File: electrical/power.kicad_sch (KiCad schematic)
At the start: 58 parts

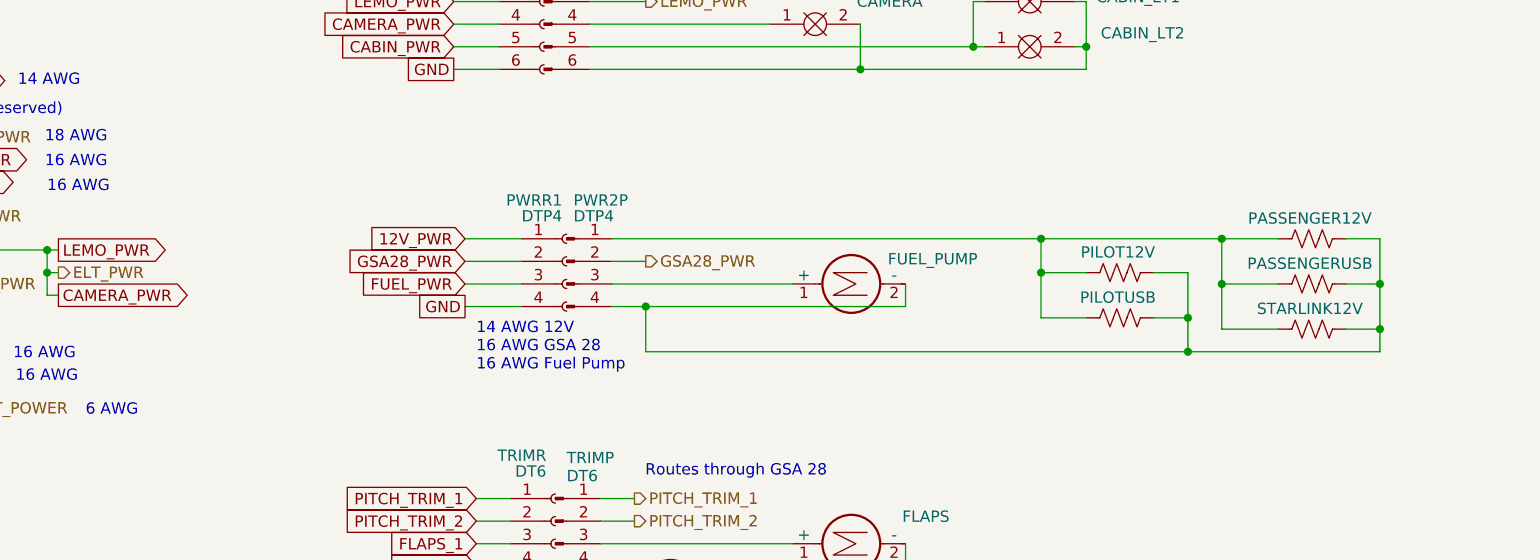
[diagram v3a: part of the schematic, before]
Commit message: Moved pilot USB to be before connector to match wiring.
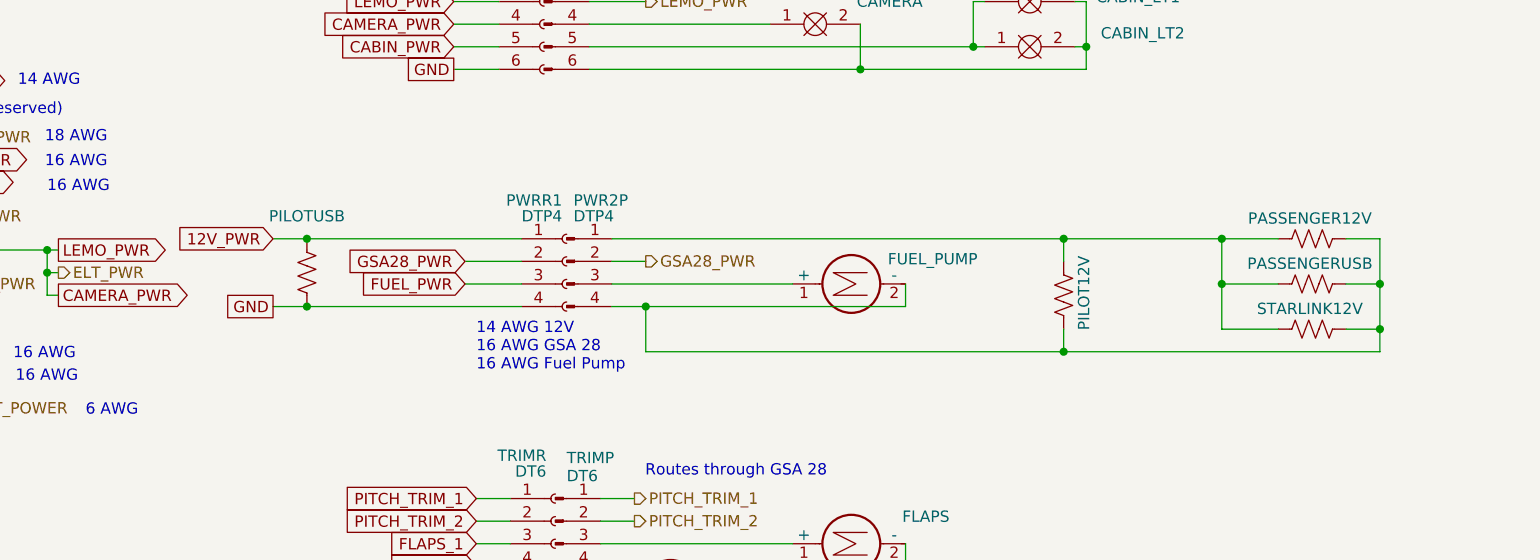
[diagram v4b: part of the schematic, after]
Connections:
- net 12V_PWR: now also PILOTUSB.2
- net GND: now also PILOTUSB.1
- net at FUEL_PUMP.2 (-), PASSENGER12V.1, PASSENGERUSB.1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: no longer PILOTUSB.1
- net at PASSENGER12V.2, PASSENGERUSB.2, PILOT12V.2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: no longer PILOTUSB.2
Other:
- moved on the sheet: PILOT12V, PILOTUSB
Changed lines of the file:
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@@
 	(title_block
 		(title "Power Distribution")
-		(date "2025-10-12")
-		(rev "1.1.8")
+		(date "2025-10-13")
+		(rev "1.1.10")
 		(company "N78HR")
 	)
@@
 	)
 	(junction
+		(at 193.04 224.79)
+		(diameter 0)
+		(color 0 0 0 0)
+	)
+	(junction
 		(at 180.34 153.67)
 		(diameter 0)
@@
 	)
 	(junction
-		(at 190.5 215.9)
-		(diameter 0)
-		(color 0 0 0 0)
-	)
-	(junction
 		(at 69.85 283.21)
 		(diameter 0)
@@
 	)
 	(junction
-		(at 207.01 220.98)
-		(diameter 0)
-		(color 0 0 0 0)
-	)
-	(junction
 		(at 99.06 341.63)
 		(diameter 0)
@@
 	)
 	(junction
+		(at 107.95 219.71)
+		(diameter 0)
+		(color 0 0 0 0)
+	)
+	(junction
 		(at 86.36 350.52)
 		(diameter 0)
@@
 	)
 	(junction
+		(at 107.95 212.09)
+		(diameter 0)
+		(color 0 0 0 0)
+	)
+	(junction
 		(at 162.56 22.86)
 		(diameter 0)
@@
 	)
 	(junction
-		(at 190.5 212.09)
-		(diameter 0)
-		(color 0 0 0 0)
-	)
-	(junction
 		(at 167.64 85.09)
 		(diameter 0)
@@
 	)
 	(junction
-		(at 207.01 224.79)
-		(diameter 0)
-		(color 0 0 0 0)
-	)
-	(junction
 		(at 86.36 336.55)
 		(diameter 0)
@@
 		(color 0 0 0 0)
 	)
+	(junction
+		(at 193.04 212.09)
+		(diameter 0)
+		(color 0 0 0 0)
+	)
 	(no_connect
 		(at 166.37 39.37)
@@
 	(wire
 		(pts
-			(xy 125.73 212.09) (xy 132.08 212.09)
+			(xy 104.14 212.09) (xy 107.95 212.09)
 		)
 		(stroke
@@
 	(wire
 		(pts
-			(xy 207.01 224.79) (xy 228.6 224.79)
+			(xy 146.05 224.79) (xy 193.04 224.79)
 		)
 		(stroke
@@
 	(wire
 		(pts
-			(xy 190.5 215.9) (xy 190.5 212.09)
-		)
-		(stroke
-			(width 0)
-			(type default)
-		)
-	)
-	(wire
-		(pts
 			(xy 195.58 193.04) (xy 195.58 190.5)
 		)
@@
 	(wire
 		(pts
-			(xy 190.5 220.98) (xy 195.58 220.98)
-		)
-		(stroke
-			(width 0)
-			(type default)
-		)
-	)
-	(wire
-		(pts
 			(xy 133.35 80.01) (xy 167.64 80.01)
 		)
@@
 	(wire
 		(pts
-			(xy 190.5 215.9) (xy 190.5 220.98)
-		)
-		(stroke
-			(width 0)
-			(type default)
-		)
-	)
-	(wire
-		(pts
 			(xy 106.68 314.96) (xy 102.87 314.96)
 		)
@@
 	(wire
 		(pts
+			(xy 107.95 212.09) (xy 132.08 212.09)
+		)
+		(stroke
+			(width 0)
+			(type default)
+		)
+	)
+	(wire
+		(pts
 			(xy 86.36 381) (xy 116.84 381)
 		)
@@
 	(wire
 		(pts
-			(xy 203.2 220.98) (xy 207.01 220.98)
-		)
-		(stroke
-			(width 0)
-			(type default)
-		)
-	)
-	(wire
-		(pts
 			(xy 162.56 102.87) (xy 166.37 102.87)
 		)
@@
 	(wire
 		(pts
-			(xy 125.73 219.71) (xy 132.08 219.71)
+			(xy 104.14 219.71) (xy 107.95 219.71)
 		)
 		(stroke
@@
 	(wire
 		(pts
-			(xy 142.24 212.09) (xy 190.5 212.09)
+			(xy 142.24 212.09) (xy 193.04 212.09)
 		)
 		(stroke
@@
 	(wire
 		(pts
-			(xy 57.15 95.25) (xy 62.23 95.25)
+			(xy 193.04 222.25) (xy 193.04 224.79)
 		)
 		(stroke
@@
 	(wire
 		(pts
-			(xy 203.2 215.9) (xy 207.01 215.9)
+			(xy 57.15 95.25) (xy 62.23 95.25)
 		)
 		(stroke
@@
 	(wire
 		(pts
-			(xy 195.58 215.9) (xy 190.5 215.9)
+			(xy 161.29 50.8) (xy 166.37 50.8)
 		)
 		(stroke
@@
 	(wire
 		(pts
-			(xy 161.29 50.8) (xy 166.37 50.8)
+			(xy 57.15 54.61) (xy 62.23 54.61)
 		)
 		(stroke
@@
 	(wire
 		(pts
-			(xy 57.15 54.61) (xy 62.23 54.61)
+			(xy 168.91 157.48) (xy 167.64 157.48)
 		)
 		(stroke
@@
 	(wire
 		(pts
-			(xy 168.91 157.48) (xy 167.64 157.48)
+			(xy 72.39 92.71) (xy 74.93 92.71)
 		)
 		(stroke
@@
 	(wire
 		(pts
-			(xy 72.39 92.71) (xy 74.93 92.71)
+			(xy 139.7 180.34) (xy 146.05 180.34)
 		)
 		(stroke
@@
 	(wire
 		(pts
-			(xy 139.7 180.34) (xy 146.05 180.34)
+			(xy 55.88 293.37) (xy 58.42 293.37)
 		)
 		(stroke
@@
 	(wire
 		(pts
-			(xy 55.88 293.37) (xy 58.42 293.37)
+			(xy 101.6 367.03) (xy 101.6 336.55)
 		)
 		(stroke
@@
 	(wire
 		(pts
-			(xy 101.6 367.03) (xy 101.6 336.55)
+			(xy 193.04 214.63) (xy 193.04 212.09)
 		)
 		(stroke
@@
 	(wire
 		(pts
+			(xy 107.95 219.71) (xy 132.08 219.71)
+		)
+		(stroke
+			(width 0)
+			(type default)
+		)
+	)
+	(wire
+		(pts
 			(xy 55.88 295.91) (xy 58.42 295.91)
 		)
@@
 	(wire
 		(pts
+			(xy 193.04 212.09) (xy 210.82 212.09)
+		)
+		(stroke
+			(width 0)
+			(type default)
+		)
+	)
+	(wire
+		(pts
 			(xy 57.15 173.99) (xy 63.5 173.99)
 		)
@@
 	(wire
 		(pts
-			(xy 207.01 215.9) (xy 207.01 220.98)
-		)
-		(stroke
-			(width 0)
-			(type default)
-		)
-	)
-	(wire
-		(pts
 			(xy 72.39 100.33) (xy 74.93 100.33)
 		)
@@
 	(wire
 		(pts
+			(xy 193.04 224.79) (xy 228.6 224.79)
+		)
+		(stroke
+			(width 0)
+			(type default)
+		)
+	)
+	(wire
+		(pts
 			(xy 100.33 339.09) (xy 106.68 339.09)
 		)
@@
 	(wire
 		(pts
-			(xy 146.05 224.79) (xy 207.01 224.79)
-		)
-		(stroke
-			(width 0)
-			(type default)
-		)
-	)
-	(wire
-		(pts
 			(xy 57.15 63.5) (xy 62.23 63.5)
 		)
@@
 	(wire
 		(pts
-			(xy 190.5 212.09) (xy 210.82 212.09)
-		)
-		(stroke
-			(width 0)
-			(type default)
-		)
-	)
-	(wire
-		(pts
 			(xy 80.01 339.09) (xy 99.06 339.09)
 		)
@@
 		)
 	)
-	(wire
-		(pts
-			(xy 207.01 220.98) (xy 207.01 224.79)
-		)
-		(stroke
-			(width 0)
-			(type default)
-		)
-	)
 	(global_label "CABIN_PWR"
 		(shape output)
@@
 	(global_label "12V_PWR"
 		(shape input)
-		(at 125.73 212.09 180)
+		(at 104.14 212.09 180)
 		(fields_autoplaced yes)
 		(effects
@@
 		)
 		(property "Intersheetrefs" "${INTERSHEET_REFS}"
-			(at 114.2782 212.09 0)
+			(at 92.6882 212.09 0)
 			(effects
 				(font
@@
 	(global_label "GND"
 		(shape passive)
-		(at 125.73 219.71 180)
+		(at 104.14 219.71 180)
 		(fields_autoplaced yes)
 		(effects
@@
 		)
 		(property "Intersheetrefs" "${INTERSHEET_REFS}"
-			(at 119.9856 219.71 0)
+			(at 98.3956 219.71 0)
 			(effects
 				(font
@@
 	(symbol
 		(lib_id "Device:R_US")
-		(at 199.39 215.9 270)
+		(at 193.04 218.44 180)
 		(unit 1)
 		(exclude_from_sim no)
@@
 		(dnp no)
 		(property "Reference" "PILOT12V"
-			(at 199.136 213.614 90)
+			(at 195.326 218.186 90)
 			(effects
 				(font
@@
 		)
 		(property "Value" "R_US"
-			(at 199.39 212.09 90)
+			(at 196.85 218.44 90)
 			(effects
 				(font
@@
 		)
 		(property "Footprint" ""
-			(at 199.136 216.916 90)
+			(at 192.024 218.186 90)
 			(effects
 				(font
@@
 		)
 		(property "Datasheet" "~"
-			(at 199.39 215.9 0)
+			(at 193.04 218.44 0)
 			(effects
 				(font
@@
 		)
 		(property "Description" "Resistor, US symbol"
-			(at 199.39 215.9 0)
+			(at 193.04 218.44 0)
 			(effects
 				(font
@@
 	(symbol
 		(lib_id "Device:R_US")
-		(at 199.39 220.98 270)
+		(at 107.95 215.9 180)
 		(unit 1)
 		(exclude_from_sim no)
@@
 		(dnp no)
 		(property "Reference" "PILOTUSB"
-			(at 199.136 218.694 90)
+			(at 107.95 209.55 0)
 			(effects
 				(font
@@
 		)
 		(property "Value" "R_US"
-			(at 199.39 217.17 90)
+			(at 111.76 215.9 90)
 			(effects
 				(font
@@
 		)
 		(property "Footprint" ""
-			(at 199.136 221.996 90)
+			(at 106.934 215.646 90)
 			(effects
 				(font
@@
 		)
 		(property "Datasheet" "~"
-			(at 199.39 220.98 0)
+			(at 107.95 215.9 0)
 			(effects
 				(font
@@
 		)
 		(property "Description" "Resistor, US symbol"
-			(at 199.39 220.98 0)
+			(at 107.95 215.9 0)
 			(effects
 				(font

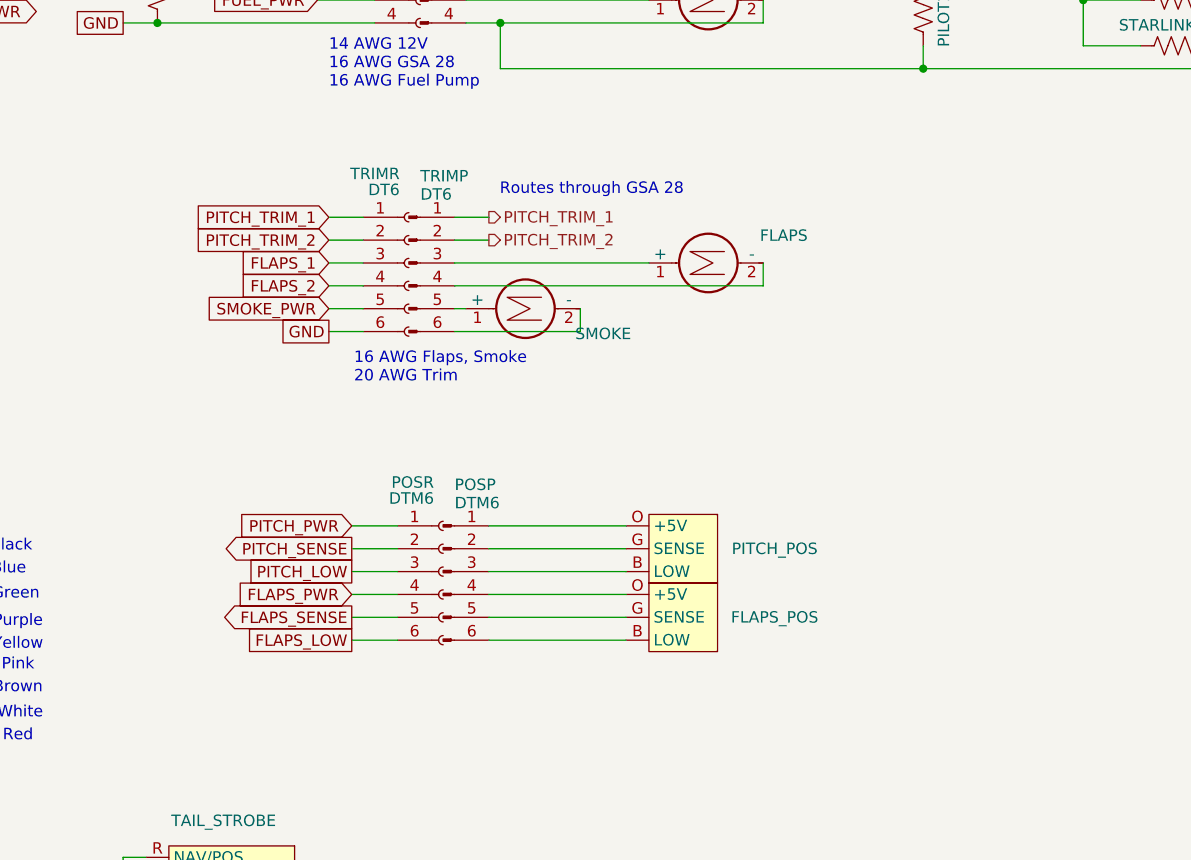
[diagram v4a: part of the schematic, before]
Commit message: Moved trim power to ray allen connector
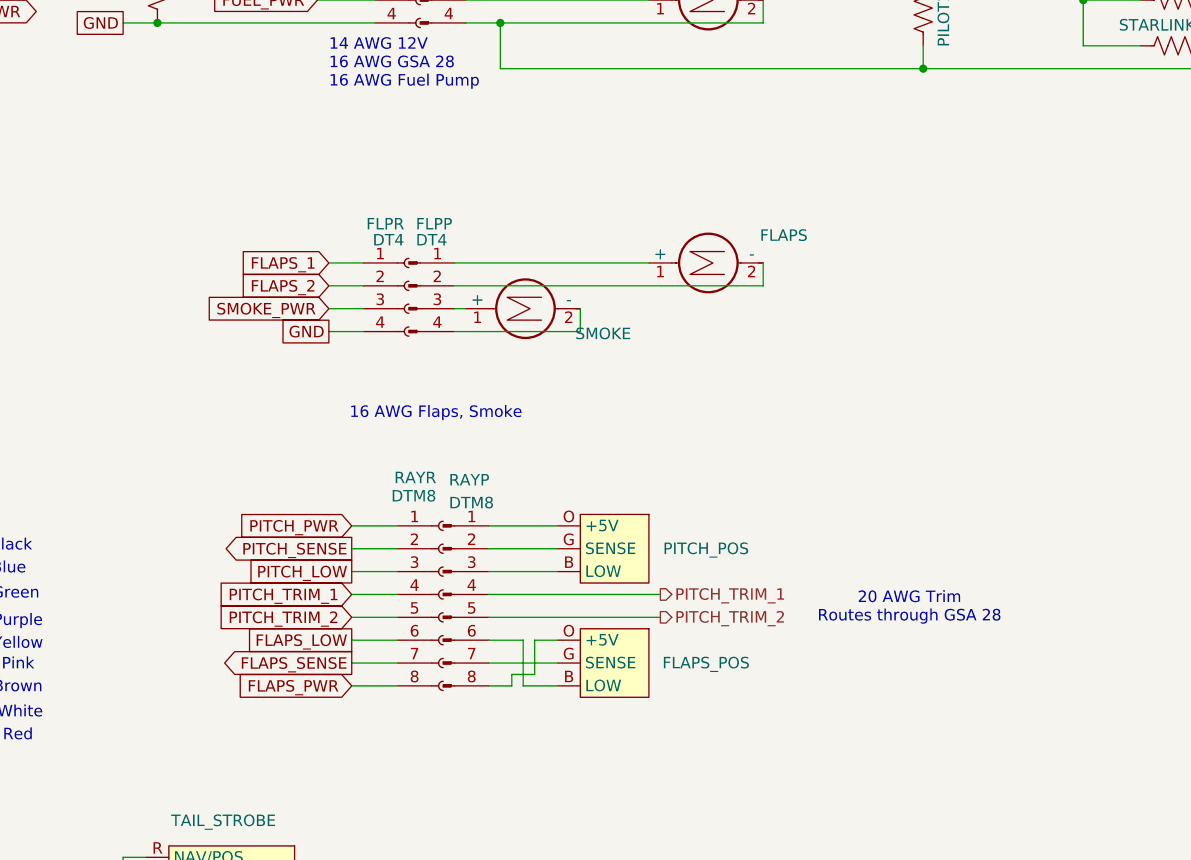
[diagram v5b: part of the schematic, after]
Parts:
- removed POSP: DTM6, symbol Connector:Conn_01x06_Pin
- removed POSR: DTM6, symbol Connector:Conn_01x06_Socket
- removed TRIMP: DT6, symbol Connector:Conn_01x06_Pin
- removed TRIMR: DT6, symbol Connector:Conn_01x06_Socket
- added FLPP: DT4, symbol Connector:Conn_01x04_Pin
- added FLPR: DT4, symbol Connector:Conn_01x04_Socket
- added RAYP: DTM8, symbol Connector:Conn_01x08_Pin
- added RAYR: DTM8, symbol Connector:Conn_01x08_Socket
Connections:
- net FLAPS_1: now also FLPR.1 (Pin_1)
- net FLAPS_2: now also FLPR.2 (Pin_2)
- net FLAPS_LOW: now also RAYR.6 (Pin_6)
- net FLAPS_PWR: now also RAYR.8 (Pin_8)
- net FLAPS_SENSE: now also RAYR.7 (Pin_7)
- net GND: now also FLPR.4 (Pin_4)
- net PITCH_LOW: now also RAYR.3 (Pin_3)
- net PITCH_PWR: now also RAYR.1 (Pin_1)
- net PITCH_SENSE: now also RAYR.2 (Pin_2)
- net PITCH_TRIM_1: now also RAYP.4 (Pin_4), RAYR.4 (Pin_4)
- net PITCH_TRIM_2: now also RAYP.5 (Pin_5), RAYR.5 (Pin_5)
- net SMOKE_PWR: now also FLPR.3 (Pin_3)
- net at FLAPS.1 (+): now also FLPP.1 (Pin_1)
- net at FLAPS.2 (-): now also FLPP.2 (Pin_2)
- net at FLAPS_POS.B (LOW): now also RAYP.6 (Pin_6)
- net at FLAPS_POS.G (SENSE): now also RAYP.7 (Pin_7)
- net at FLAPS_POS.O (+5V): now also RAYP.8 (Pin_8)
- net at SMOKE.1 (+): now also FLPP.3 (Pin_3)
- net at SMOKE.2 (-): now also FLPP.4 (Pin_4)
- net at PITCH_POS.O (+5V): now also RAYP.1 (Pin_1)
- net at PITCH_POS.G (SENSE): now also RAYP.2 (Pin_2)
- net at PITCH_POS.B (LOW): now also RAYP.3 (Pin_3)
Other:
- note added: "16 AWG Flaps, Smoke"
- note added: "20 AWG Trim Routes through GSA 28"
- note removed: "16 AWG Flaps, Smoke 20 AWG Trim"
- note removed: "Routes through GSA 28"
- moved on the sheet: FLAPS_POS, PITCH_POS
